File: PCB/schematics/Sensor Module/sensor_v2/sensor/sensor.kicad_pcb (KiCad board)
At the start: 2 copper layers, 14 parts, among them IC1 LM358DT

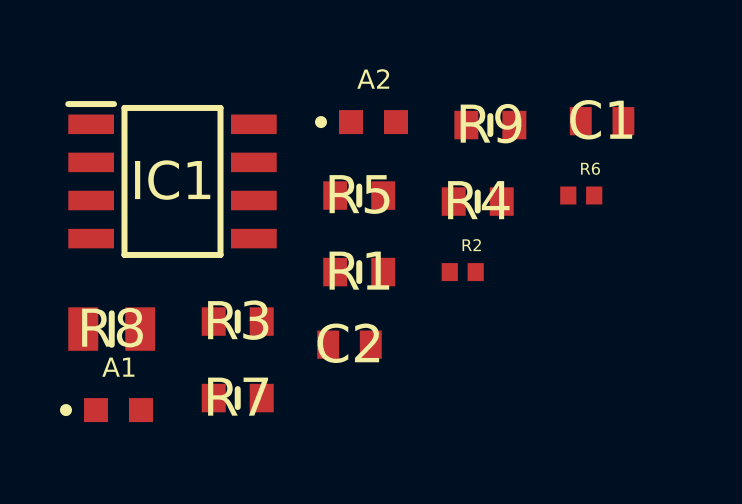
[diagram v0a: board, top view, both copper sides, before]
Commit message: Week 5 submission, with analog sensor with pcb updated
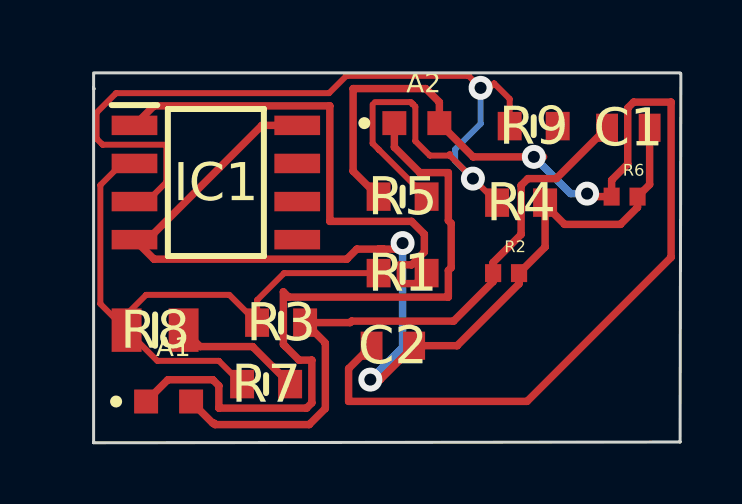
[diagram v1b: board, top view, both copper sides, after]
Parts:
- moved A1 1.69 mm to (121.0, 103.9)
- moved R2 1.45 mm to (132.3, 99.6)
- moved R4 1.45 mm to (132.8, 97.2)
- moved C2 1.45 mm to (128.5, 102.0)
- moved IC1 1.45 mm to (122.6, 96.6)
- moved R5 1.45 mm to (128.8, 97.0), turned to 180 degrees
- moved R6 1.45 mm to (136.2, 97.0)
- moved A2 1.45 mm to (129.3, 94.6)
- moved R1 1.45 mm to (128.8, 99.6)
- moved R3 1.45 mm to (124.8, 101.2)
- moved R8 1.45 mm to (120.6, 101.5)
- moved R9 1.45 mm to (133.2, 94.7)
- moved R7 1.05 mm to (124.3, 103.3)
- moved C1 0.90 mm to (136.4, 94.7)
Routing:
- net Vout2: track 0.00 -> 39.6 mm, vias 0 -> 2
- net +3v3: track 0.00 -> 37.2 mm, vias 0 -> 2
- net IN1+: track 0.00 -> 35.2 mm, vias 0 -> 2
- net 3v3: track 0.00 -> 23.9 mm
- net Vout1: track 0.00 -> 22.2 mm
- net IN1-: track 0.00 -> 21.9 mm
- net Vdiff: track 0.00 -> 17.2 mm
- net +5v: track 0.00 -> 4.30 mm
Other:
- board outline added: 19.6 x 12.3 mm
